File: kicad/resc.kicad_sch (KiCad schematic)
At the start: 40 parts, among them J1 CAN, J10 LED2, J2 HALL, J3 COMM, J4 SERVO, J5 SWD, J8 POWER BTN, J9 LED1, SW1 SENSOR_VOLTAGE

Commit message: checking shunt footprints
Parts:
- TP1: renamed from TP6; footprint (none) -> footprints:TestPoint_Pad_7.0x7.0mm
- TP2: renamed from TP7; footprint (none) -> footprints:TestPoint_Pad_7.0x7.0mm
- renumbered C56 to C1, C50 to C2, C65 to C3, C66 to C4, D4 to D1, D5 to D2, D6 to D4, D8 to D5, D7 to D6, D9 to D7, J8 to J4, J4 to J5, J5 to J6, J9 to J7, J10 to J8, R35 to R1, R40 to R10, R39 to R11, R41 to R12, R42 to R13, R45 to R14, R43 to R15, R44 to R16, R46 to R17, R32 to R2, R33 to R3, R34 to R4, R30 to R5, R31 to R6, R29 to R7, R38 to R8, R28 to R9
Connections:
- net GND: no longer J4.1 (Pin_1)
- net VDD: now also J4.1 (Pin_1)

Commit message: routing gate driver
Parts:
- removed TP1: + SUPPLY, footprints:TestPoint_Pad_7.0x7.0mm, symbol Connector:TestPoint
- removed TP2: - SUPPLY, footprints:TestPoint_Pad_7.0x7.0mm, symbol Connector:TestPoint
- added H1, H2, H3, H4: MountingHole, MountingHole:MountingHole_3.2mm_M3, symbol Mechanical:MountingHole
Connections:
- net GND: now also J4.1 (Pin_1)
- net VDD: no longer J4.1 (Pin_1)

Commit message: revert to v6.05
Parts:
- added R24: 0R, Resistor_SMD:R_0402_1005Metric, symbol Device:R_US
- added TP1: DRV_CE, TestPoint:TestPoint_Pad_D1.0mm, symbol Connector:TestPoint
- added TP10: nFAULT, TestPoint:TestPoint_Pad_D1.0mm, symbol Connector:TestPoint
- added TP11: EN_GATE, TestPoint:TestPoint_Pad_D1.0mm, symbol Connector:TestPoint
- added TP2: SENS_FILT, TestPoint:TestPoint_Pad_D1.0mm, symbol Connector:TestPoint
- added TP8: BUCK_V, TestPoint:TestPoint_Pad_D1.0mm, symbol Connector:TestPoint
- added TP9: SHUTDOWN, TestPoint:TestPoint_Pad_D1.0mm, symbol Connector:TestPoint
- D4, D5, D6, D7: footprint Diode_SMD:D_SOD-323 -> Diode_SMD:D_SOD-323_HandSoldering
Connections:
- net GND: no longer J4.1 (Pin_1)
- net Gate Driver/EN_GATE: now also TP11.1
- net Gate Driver/SENS_FILTERED: now also TP2.1
- net SHUTDOWN: now also TP9.1
- net VDD: now also J4.1 (Pin_1)
- net at D5.1 (K), R12.2, R15.1: now also R24.1
- net EN_BUCK renamed DRV_CE
- net DRV_CE: now also R24.2, TP1.1
- new net Gate Driver/DRV_BUCK_OUT: TP8.1
- new net Gate Driver/nFAULT: TP10.1
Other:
- sheet Shunt Amplifiers renamed MOSFETs
- sheet Gate Driver ports: added DRV_BUCK_OUT, DRV_CE, SCK, nFAULT; removed EN_BUCK, FAULT, SCLK
- sheet Power ports: added DRV_BUCK_OUT; removed none
- moved on the sheet: C3, D6, J4, J7, J8, R14, R17

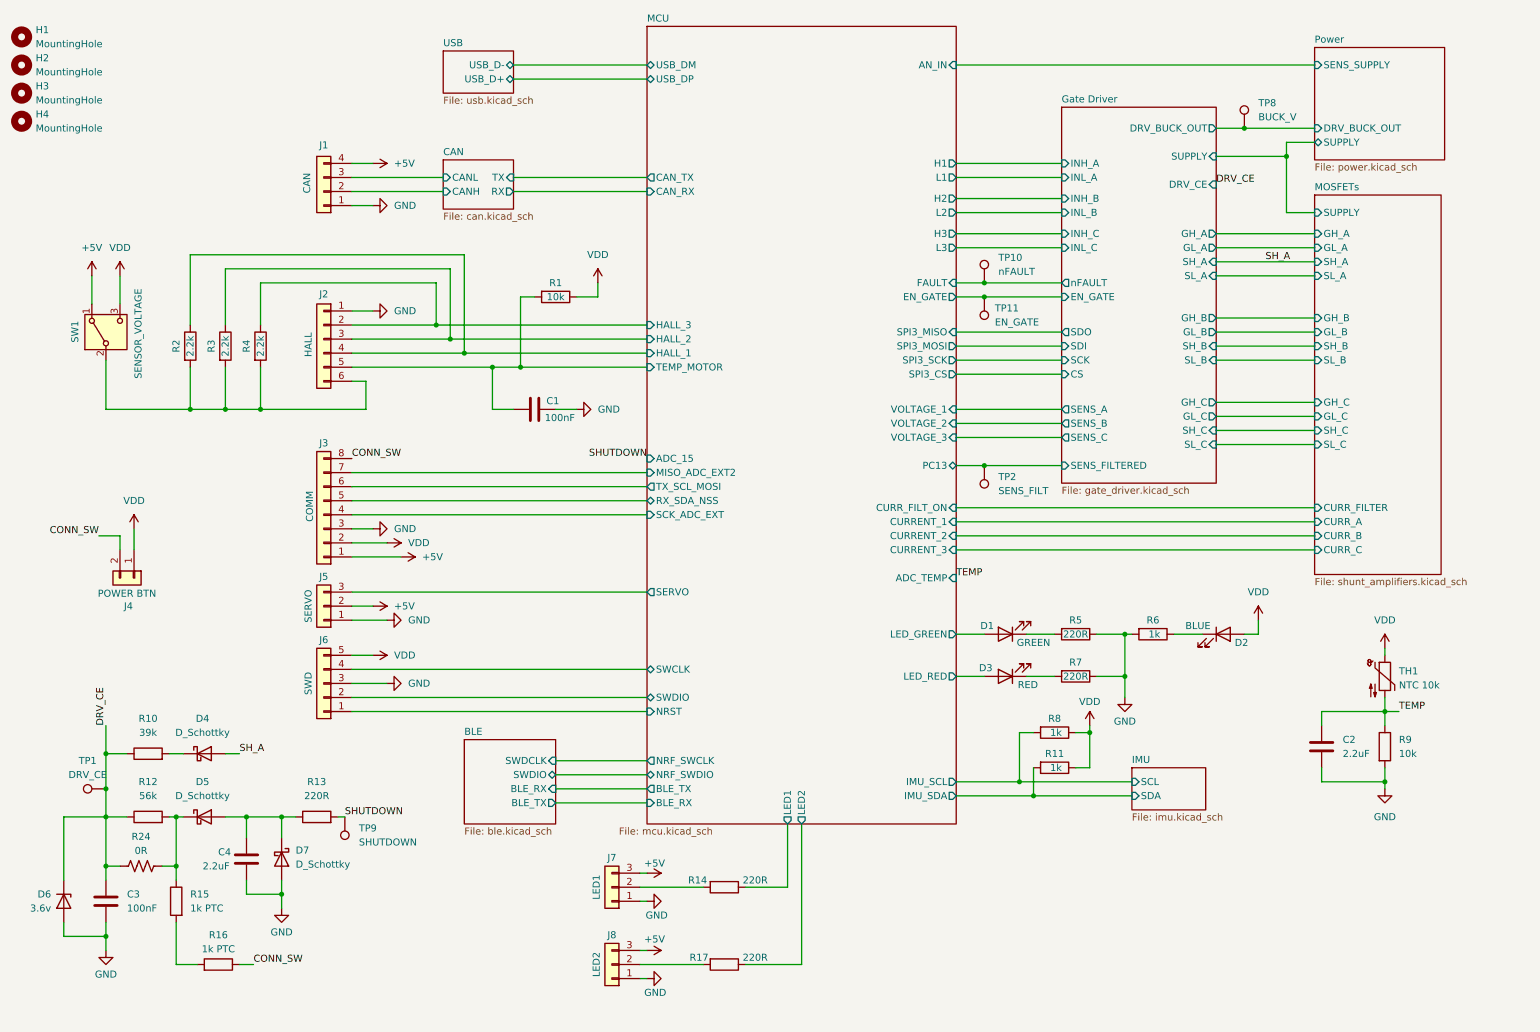
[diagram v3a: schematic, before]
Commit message: gate driver mostly schematic'd and pcb started
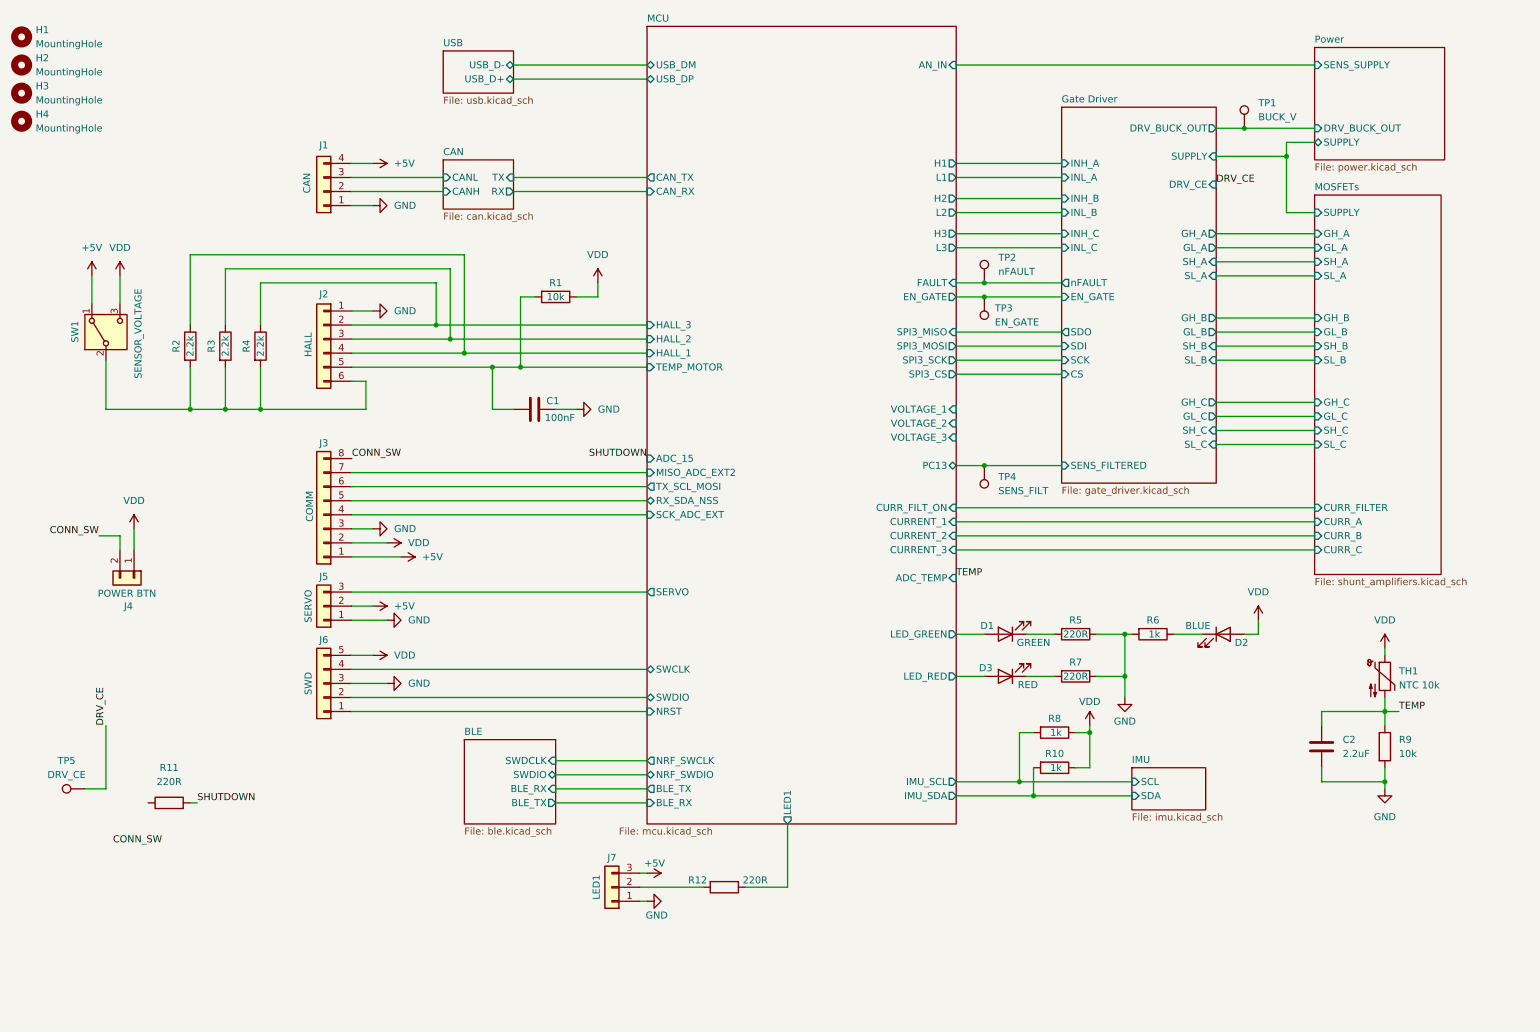
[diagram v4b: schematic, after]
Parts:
- removed C3: 100nF, Capacitor_SMD:C_0402_1005Metric, symbol Device:C
- removed C4: 2.2uF, Capacitor_SMD:C_0402_1005Metric, symbol Device:C
- removed D4, D5, D7: D_Schottky, Diode_SMD:D_SOD-323_HandSoldering, symbol Device:D_Schottky
- removed D6: 3.6v, Diode_SMD:D_SOD-323_HandSoldering, symbol Device:D_Zener
- removed J8: LED2, Connector_JST:JST_PH_B3B-PH-K_1x03_P2.00mm_Vertical, symbol Connector_Generic:Conn_01x03
- removed R10: 39k, Resistor_SMD:R_0402_1005Metric, symbol Device:R
- removed R12: 56k, Resistor_SMD:R_0402_1005Metric, symbol Device:R
- removed R15, R16: 1k PTC, Resistor_SMD:R_0402_1005Metric, symbol Device:R
- removed R17: 220R, Resistor_SMD:R_0402_1005Metric, symbol Device:R
- removed R24: 0R, Resistor_SMD:R_0402_1005Metric, symbol Device:R_US
- removed TP9: SHUTDOWN, TestPoint:TestPoint_Pad_D1.0mm, symbol Connector:TestPoint
- renumbered R11 to R10, R13 to R11, R14 to R12, TP8 to TP1, TP10 to TP2, TP11 to TP3, TP2 to TP4, TP1 to TP5
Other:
- sheet Gate Driver ports: added none; removed SENS_A, SENS_B, SENS_C
- sheet MCU ports: added none; removed LED2
- moved on the sheet: R11, TP5

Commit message: rev3 ordered
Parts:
- removed H1, H2, H3, H4: MountingHole, MountingHole:MountingHole_3.2mm_M3, symbol Mechanical:MountingHole
- removed TP1: BUCK_V, TestPoint:TestPoint_Pad_D1.0mm, symbol Connector:TestPoint
- added C3: 100nF, Capacitor_SMD:C_0402_1005Metric, symbol Device:C
- added Q8: DMG3415U, Package_TO_SOT_SMD:SOT-23-3, symbol Device:Q_PMOS_Depletion
- added R10: 100k, Resistor_SMD:R_0402_1005Metric, symbol Device:R_US
- added R12: 10k, Resistor_SMD:R_0402_1005Metric, symbol Device:R_US
- added TP8: CONN_SW, TestPoint:TestPoint_Pad_D1.0mm, symbol Connector:TestPoint
- R1, R2, R3, R4, R5, R6, R7, R8, R9: symbol Device:R -> Device:R_US
- R11: renamed from R10; symbol Device:R -> Device:R_US
- R13: renamed from R11; symbol Device:R -> Device:R_US
- R14: renamed from R12; symbol Device:R -> Device:R_US
- TP1: renamed from TP5; value DRV_CE -> nSHDN
- TP11: renamed from TP3; value EN_GATE -> EN_DRV
- renumbered TP2 to TP10, TP4 to TP2
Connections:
- net DRV_CE is gone; now on net nSHDN: TP1.1
- net CONN_SW: now also C3.1, Q8.G, R12.2, TP8.1
- net GND: now also J4.1 (Pin_1), C3.2, R10.1
- net VDD: now also Q8.S, R12.1; no longer J4.1 (Pin_1)
- net nSHDN: now reaches R13.1
- net nSHDN: now also Q8.D, R10.2
- net Gate Driver/EN_GATE renamed Gate Driver/EN_DRV
- net SHUTDOWN renamed POWER
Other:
- sheet Gate Driver ports: added EN_DRV, VOLTAGE_A, VOLTAGE_B, VOLTAGE_C, nSHDN; removed DRV_BUCK_OUT, DRV_CE, EN_GATE
- sheet MCU ports: added CONN_SW, EN_DRV, POWER; removed ADC_15, EN_GATE
- sheet Power ports: added none; removed DRV_BUCK_OUT
- moved on the sheet: C1, D2, J4, J7, TP1
